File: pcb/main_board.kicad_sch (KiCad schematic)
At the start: 50 parts

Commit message: Further schematic capture
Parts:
- removed C?: 4.7u, symbol Device:C
- added C?: 4.7u, symbol Device:C
- J?: value DISP_OUTPUT -> TO_DISP_OUTPUT
- J?: value DISP_INPUT -> TO_DISP_INPUT
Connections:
- net GND: now also C?.2
- net at U?.15 (VDD1.8), U?.26 (VDD1.8): now also C?.1
- net ADAT_IN1_USER0: now reaches U?.3 (PE4)
- net ADAT_IN1_USER3: now reaches U?.38 (PE7)
- net ADAT_IN2_USER0: now reaches U?.39 (PE8)
- net ADAT_IN1_USER1: now reaches U?.4 (PE5)
- net ADAT_IN2_USER1: now reaches U?.40 (PE9)
- net ADAT_IN2_USER2: now reaches U?.41 (PE10)
- net ADAT_IN2_USER3: now reaches U?.42 (PE11)
- net ADAT_OUT1_USER0: now reaches U?.43 (PE12)
- net ADAT_OUT1_USER1: now reaches U?.44 (PE13)
- net ADAT_OUT1_USER2: now reaches U?.45 (PE14)
- net ADAT_OUT1_USER3: now reaches U?.46 (PE15)
- net ADAT_IN1_USER2: now reaches U?.5 (PE6)
- net GPIO_LOOPBACK: now reaches U?.61 (PD14)
- net ADAT_OUT2_USER0: now reaches U?.68 (PA9)
- net ADAT_OUT2_USER1: now reaches U?.69 (PA10)
- net ADAT_OUT2_USER2: now reaches U?.70 (PA11)
- net ADAT_OUT2_USER3: now reaches U?.71 (PA12)
- no-connect marks 46 -> 29
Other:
- moved on the sheet: C?, D?, R?

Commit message: Further schematic capture
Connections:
- net SW_SAMPLERATE: now reaches J?.7 (SW_SR)
- net SW_SAMPLERATE: now also U?.34 (PC5)
- net SW_LOOPBACK: now reaches J?.8 (SW_LB)
- net SW_LOOPBACK: now also U?.63 (PC6)
- no-connect marks 29 -> 27
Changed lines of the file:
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@@
 	(text "I^{2}C addr: 1101001=0xD2"
 		(exclude_from_sim no)
-		(at 160.02 110.998 90)
+		(at 163.068 110.744 90)
 		(effects
 			(font
@@
 	(text "I^{2}C addr: 1101000=0xD0"
 		(exclude_from_sim no)
-		(at 160.02 68.834 90)
+		(at 163.068 68.58 90)
 		(effects
 			(font
@@
 	)
 	(no_connect
-		(at 93.98 147.32)
-	)
-	(no_connect
 		(at 43.18 114.3)
 	)
@@
 	)
 	(no_connect
-		(at 93.98 144.78)
-	)
-	(no_connect
 		(at 43.18 149.86)
 	)
@@
 	(wire
 		(pts
+			(xy 93.98 147.32) (xy 111.76 147.32)
+		)
+		(stroke
+			(width 0)
+			(type default)
+		)
+	)
+	(wire
+		(pts
 			(xy 40.64 33.02) (xy 60.96 33.02)
 		)
@@
 	(wire
 		(pts
+			(xy 130.81 116.84) (xy 151.13 116.84)
+		)
+		(stroke
+			(width 0)
+			(type default)
+		)
+	)
+	(wire
+		(pts
 			(xy 147.32 148.59) (xy 147.32 151.13)
 		)
@@
 	(wire
 		(pts
+			(xy 93.98 144.78) (xy 111.76 144.78)
+		)
+		(stroke
+			(width 0)
+			(type default)
+		)
+	)
+	(wire
+		(pts
 			(xy 104.14 53.34) (xy 93.98 53.34)
 		)
@@
 	(wire
 		(pts
+			(xy 130.81 114.3) (xy 151.13 114.3)
+		)
+		(stroke
+			(width 0)
+			(type default)
+		)
+	)
+	(wire
+		(pts
 			(xy 229.87 24.13) (xy 222.25 24.13)
 		)
@@
 		)
 	)
+	(label "SW_SAMPLERATE"
+		(at 111.76 144.78 180)
+		(effects
+			(font
+				(size 1.27 1.27)
+			)
+			(justify right bottom)
+		)
+	)
 	(label "ULPI_D6"
 		(at 199.39 119.38 0)
@@
 		)
 	)
+	(label "SW_SAMPLERATE"
+		(at 130.81 114.3 0)
+		(effects
+			(font
+				(size 1.27 1.27)
+			)
+			(justify left bottom)
+		)
+	)
 	(label "ULPI_D7"
 		(at 104.14 101.6 180)
@@
 		)
 	)
+	(label "SW_LOOPBACK"
+		(at 111.76 147.32 180)
+		(effects
+			(font
+				(size 1.27 1.27)
+			)
+			(justify right bottom)
+		)
+	)
+	(label "SW_LOOPBACK"
+		(at 130.81 116.84 0)
+		(effects
+			(font
+				(size 1.27 1.27)
+			)
+			(justify left bottom)
+		)
+	)
 	(label "XTAL1"
 		(at 153.67 27.94 180)
@@
 	)
 	(symbol
+		(lib_name "Connector_Display_1")
 		(lib_id "adatv2:Connector_Display")
 		(at 157.48 71.12 0)

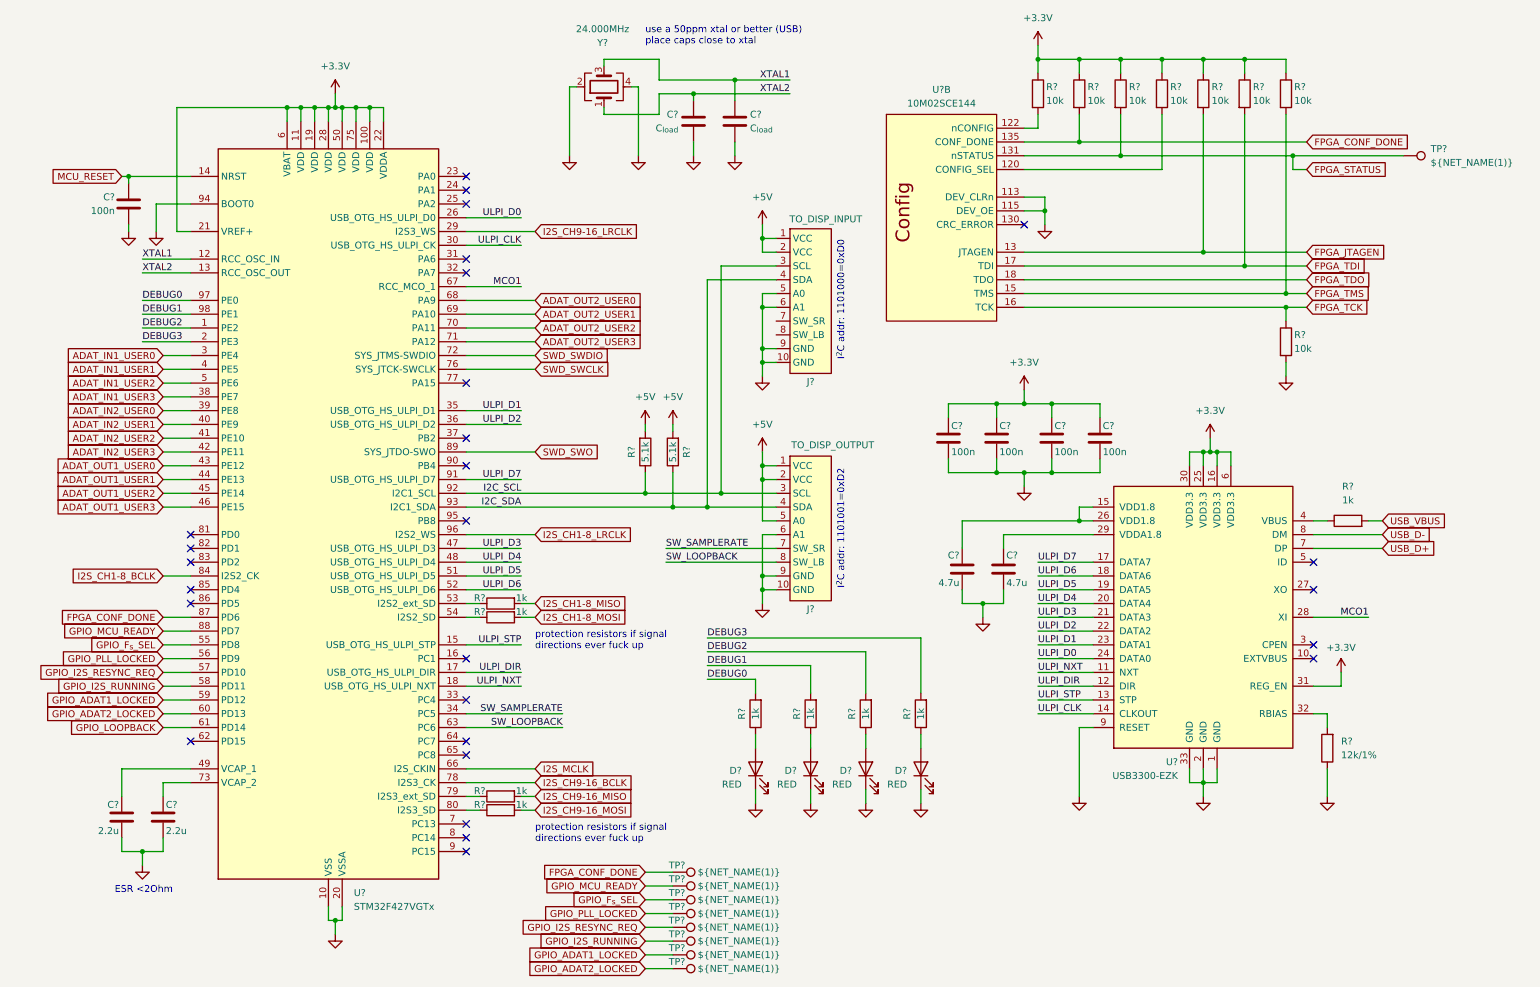
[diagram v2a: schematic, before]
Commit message: Assign most of the footprints to schematic components
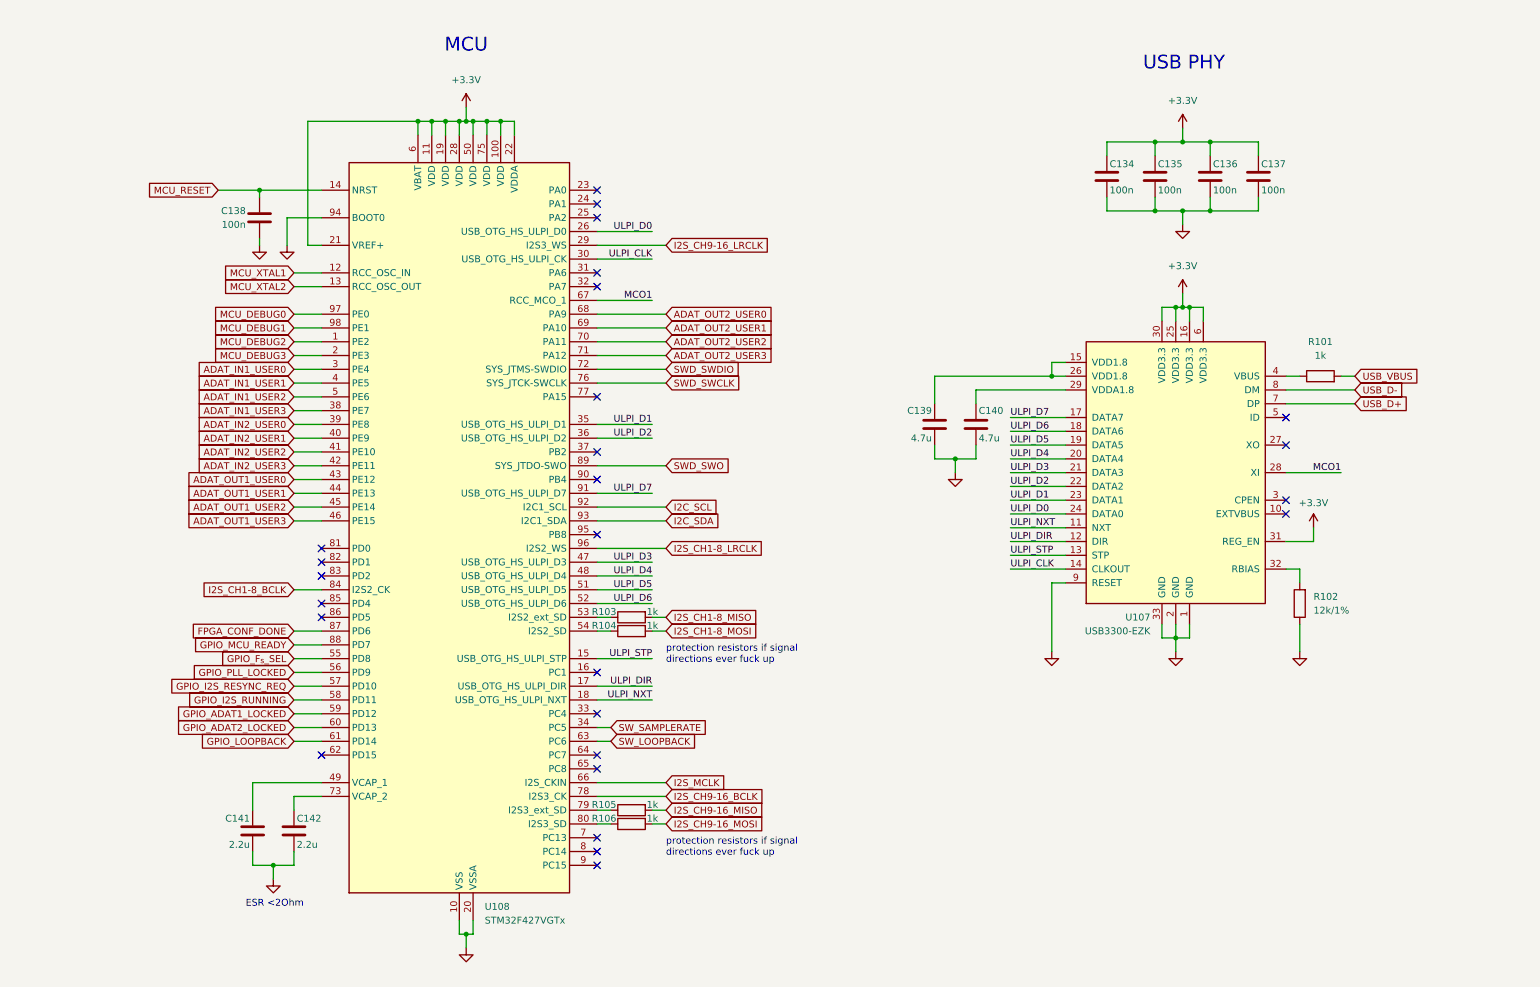
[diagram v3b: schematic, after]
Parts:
- removed C? (x2): C_{load}, symbol Device:C
- removed D? (x4): RED, symbol Device:LED
- removed J?: TO_DISP_OUTPUT, symbol adatv2:Connector_Display
- removed J?: TO_DISP_INPUT, symbol adatv2:Connector_Display
- removed R? (x8): 10k, symbol Device:R
- removed R? (x4): 1k, symbol Device:R
- removed R? (x2): 5.1k, symbol Device:R
- removed TP? (x9): ${NET_NAME(1)}, symbol Connector:TestPoint
- removed U?: 10M02SCE144, Package_QFP:EQFP-144-1EP_20x20mm_P0.5mm_EP4x4mm_ThermalVias, symbol adatv2:10M02SCE144
- removed Y?: 24.000MHz, symbol Device:Crystal_GND24
- C134, C135, C136, C137, C138, C139, C140, C141, C142: renamed from C?; footprint (none) -> Capacitor_SMD:C_0805_2012Metric_Pad1.18x1.45mm_HandSolder
- R101, R102, R103, R104, R105, R106: renamed from R?; footprint (none) -> Resistor_SMD:R_0805_2012Metric_Pad1.20x1.40mm_HandSolder
- gave numbers to parts that had none: 2
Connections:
- net DEBUG0 renamed MCU_DEBUG0
- net DEBUG1 renamed MCU_DEBUG1
- net DEBUG2 renamed MCU_DEBUG2
- net DEBUG3 renamed MCU_DEBUG3
- net XTAL1 renamed MCU_XTAL1
- net XTAL2 renamed MCU_XTAL2
- no-connect marks 27 -> 26
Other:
- note added: "MCU"
- note added: "USB PHY"
- note removed: "I^{2}C addr: 1101000=0xD0"
- note removed: "I^{2}C addr: 1101001=0xD2"
- note removed: "use a 50ppm xtal or better (USB) place caps close to xtal"
- moved on the sheet: C134, C135, C136, C137, C138, C139, C140, C141, C142, R101, R102, R103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

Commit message: Finish assigning footprints to project
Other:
- note added: "C108383"
- note added: "C117815"
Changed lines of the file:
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@@
+		)
+	)
+	(text "C108383"
+		(exclude_from_sim no)
+		(at 215.646 132.588 0)
+		(effects
+			(font
+				(size 1.27 1.27)
+			)
 		)
 	)
@@
 		)
 	)
+	(text "C117815"
+		(exclude_from_sim no)
+		(at 101.6 185.42 0)
+		(effects
+			(font
+				(size 1.27 1.27)
+			)
+		)
+	)

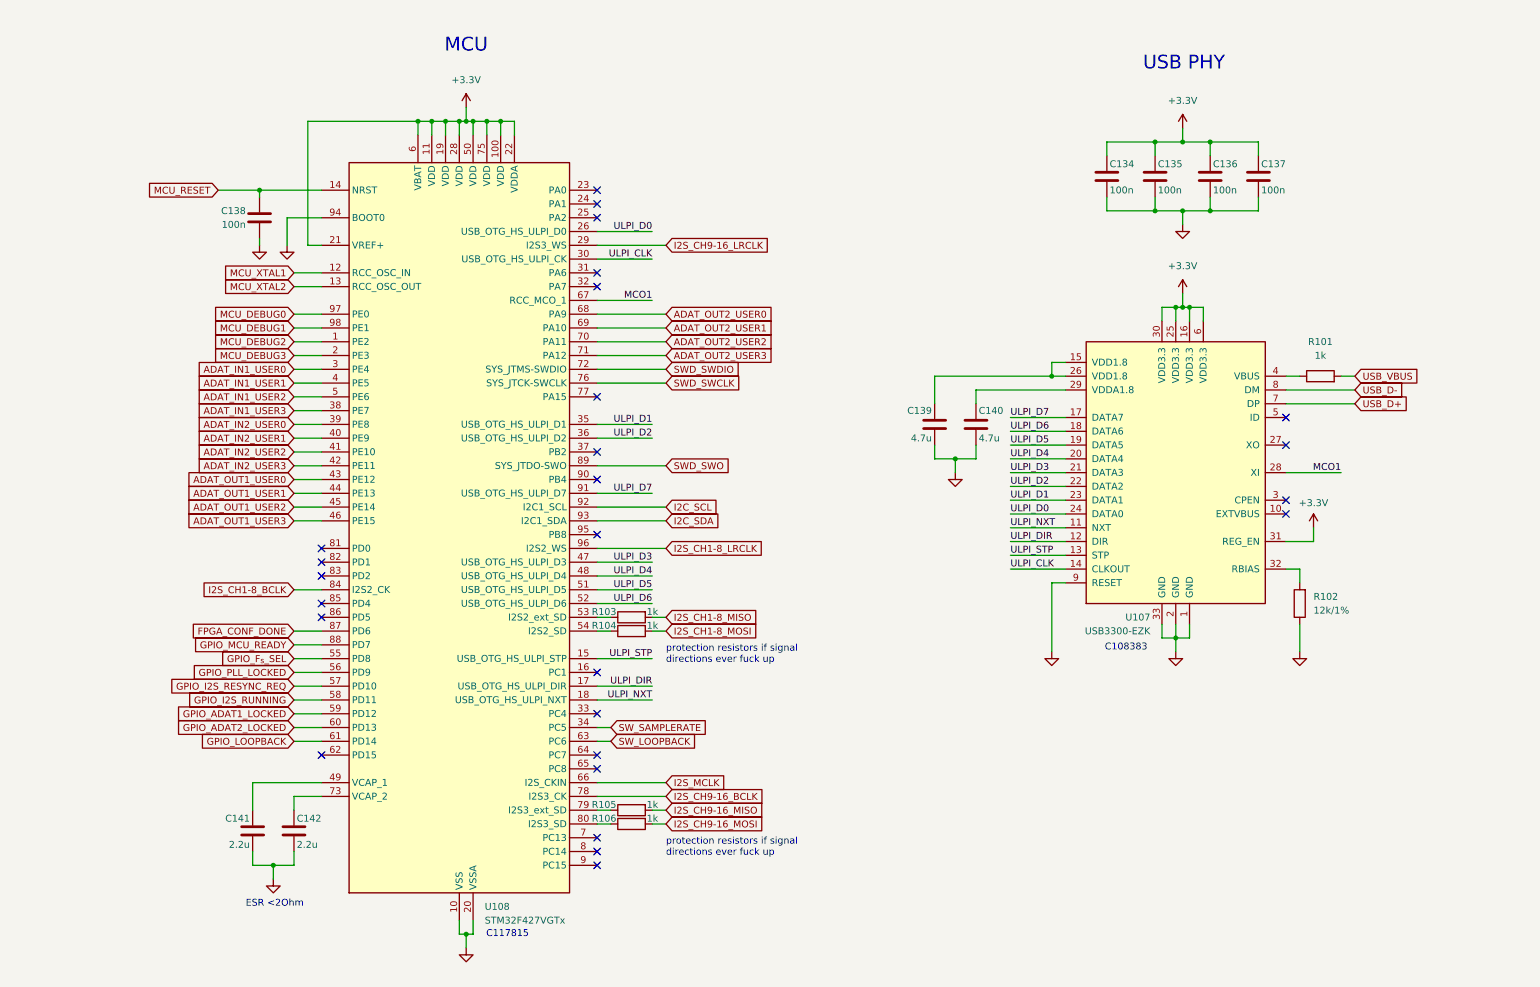
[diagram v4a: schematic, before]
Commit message: Finish drawing IO/Supply board
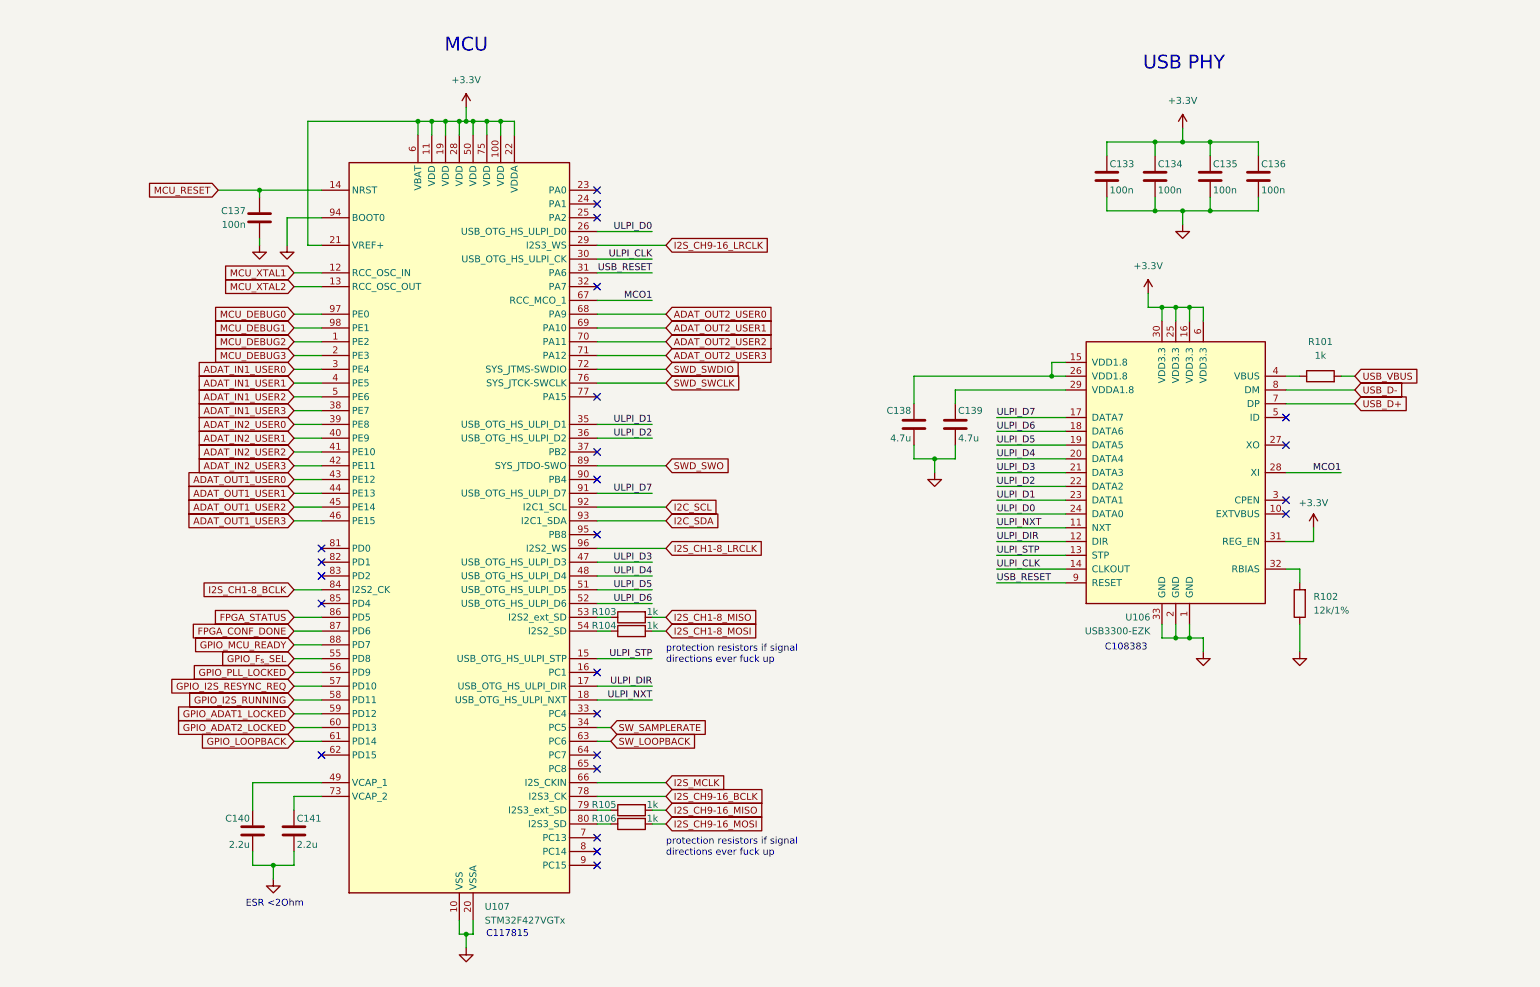
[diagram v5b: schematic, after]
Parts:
- renumbered C134 to C133, C135 to C134, C136 to C135, C137 to C136, C138 to C137, C139 to C138, C140 to C139, C141 to C140, C142 to C141, U107 to U106, U108 to U107
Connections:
- net GND: no longer U106.9 (RESET)
- net USB_RESET: now reaches U107.31 (PA6)
- net USB_RESET: now also U106.9 (RESET)
- net FPGA_STATUS: now reaches U107.86 (PD5)
- no-connect marks 26 -> 24
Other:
- moved on the sheet: C138, C139

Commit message: Add missing CAD models of I/O electronic components
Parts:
- R103, R104, R105, R106: value 1k -> 150
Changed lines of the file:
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@@
 			)
 		)
-		(property "Value" "1k"
+		(property "Value" "150"
 			(at 127.254 125.984 90)
 			(effects
@@
 			)
 		)
-		(property "Value" "1k"
+		(property "Value" "150"
 			(at 127.254 164.084 90)
 			(effects
@@
 			)
 		)
-		(property "Value" "1k"
+		(property "Value" "150"
 			(at 127.254 161.544 90)
 			(effects
@@
 			)
 		)
-		(property "Value" "1k"
+		(property "Value" "150"
 			(at 127.254 128.524 90)
 			(effects

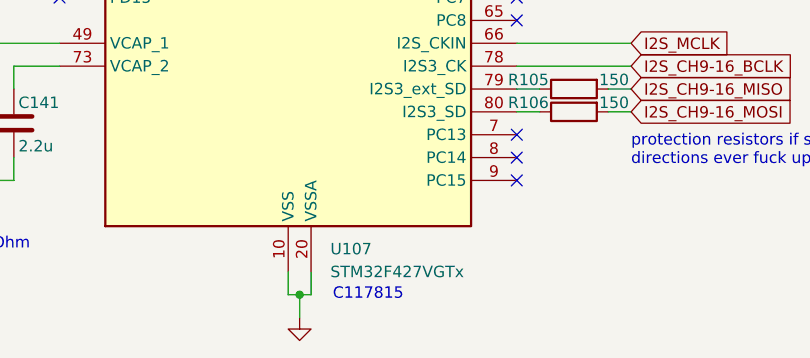
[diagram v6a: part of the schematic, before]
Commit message: Assign FPGA pins, change MCU to STM32F429VET6
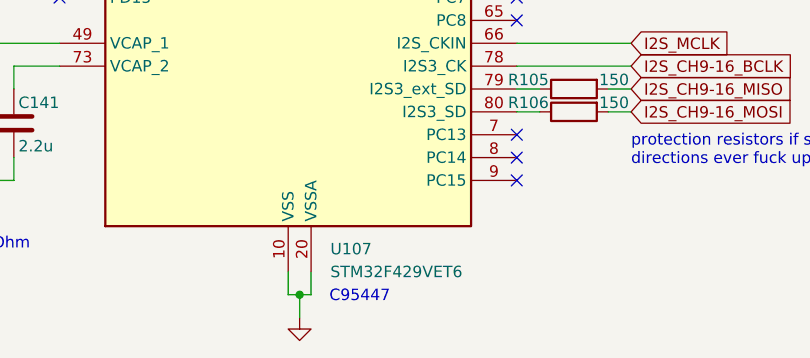
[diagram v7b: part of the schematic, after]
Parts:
- U107: value STM32F427VGTx -> STM32F429VET6
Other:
- note added: "C95447"
- note removed: "C117815"
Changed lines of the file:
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@@
 		)
 	)
-	(text "C117815"
+	(text "C95447"
 		(exclude_from_sim no)
-		(at 101.6 185.42 0)
+		(at 97.282 185.674 0)
 		(effects
 			(font
 				(size 1.27 1.27)
 			)
+			(justify left)
 		)
 	)
@@
 			)
 		)
-		(property "Value" "STM32F427VGTx"
+		(property "Value" "STM32F429VET6"
 			(at 97.3933 182.88 0)
 			(effects
